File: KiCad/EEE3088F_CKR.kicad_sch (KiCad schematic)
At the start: 0 parts

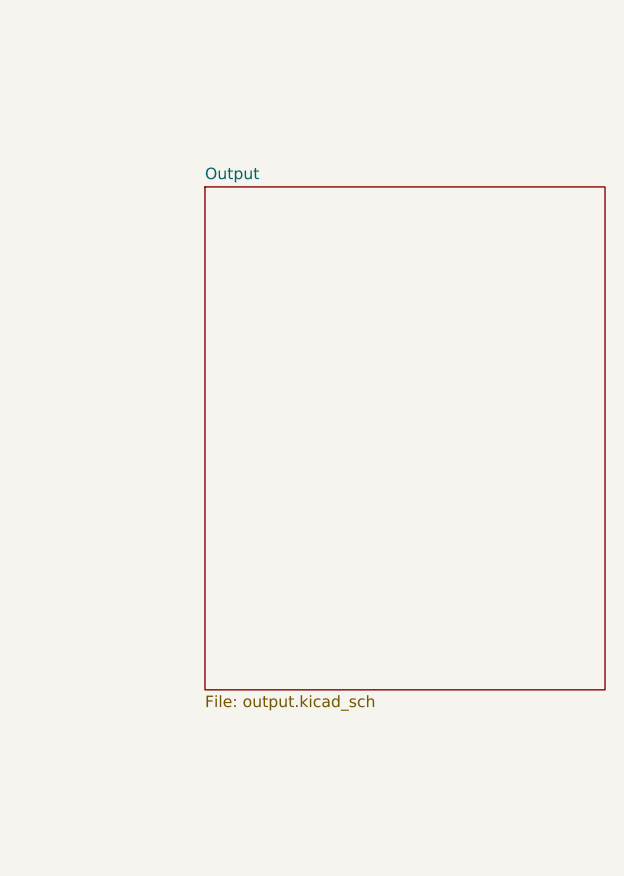
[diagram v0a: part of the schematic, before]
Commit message: added EEPROM
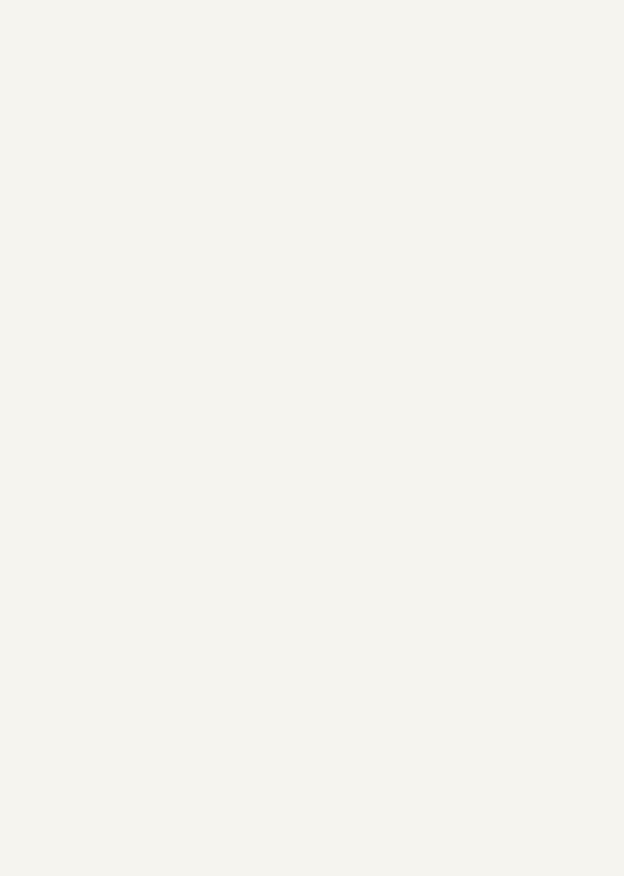
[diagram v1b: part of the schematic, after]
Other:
- removed sheet Output
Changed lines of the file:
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@@
 (kicad_sch (version 20230121) (generator eeschema)
   (paper "A4")
-  (sheet (at 210.82 77.47) (size 44.45 55.88) (fields_autoplaced)
-    (stroke (width 0.1524) (type solid))
-    (fill (color 0 0 0 0.0000))
-    (property "Sheetname" "Output" (at 210.82 76.7584 0)
-      (effects (font (size 1.27 1.27)) (justify left bottom))
-    )
-    (property "Sheetfile" "output.kicad_sch" (at 210.82 133.9346 0)
-      (effects (font (size 1.27 1.27)) (justify left top))
-    )
-    (instances
-      (project "EEE3088F_CKR"
-        (path "/31e5d740-f3fb-4029-be8d-dfdc4f653d72" (page "5"))
-      )
-    )
-  )
   (sheet (at 135.89 53.34) (size 33.02 95.25) (fields_autoplaced)
     (stroke (width 0.1524) (type solid))

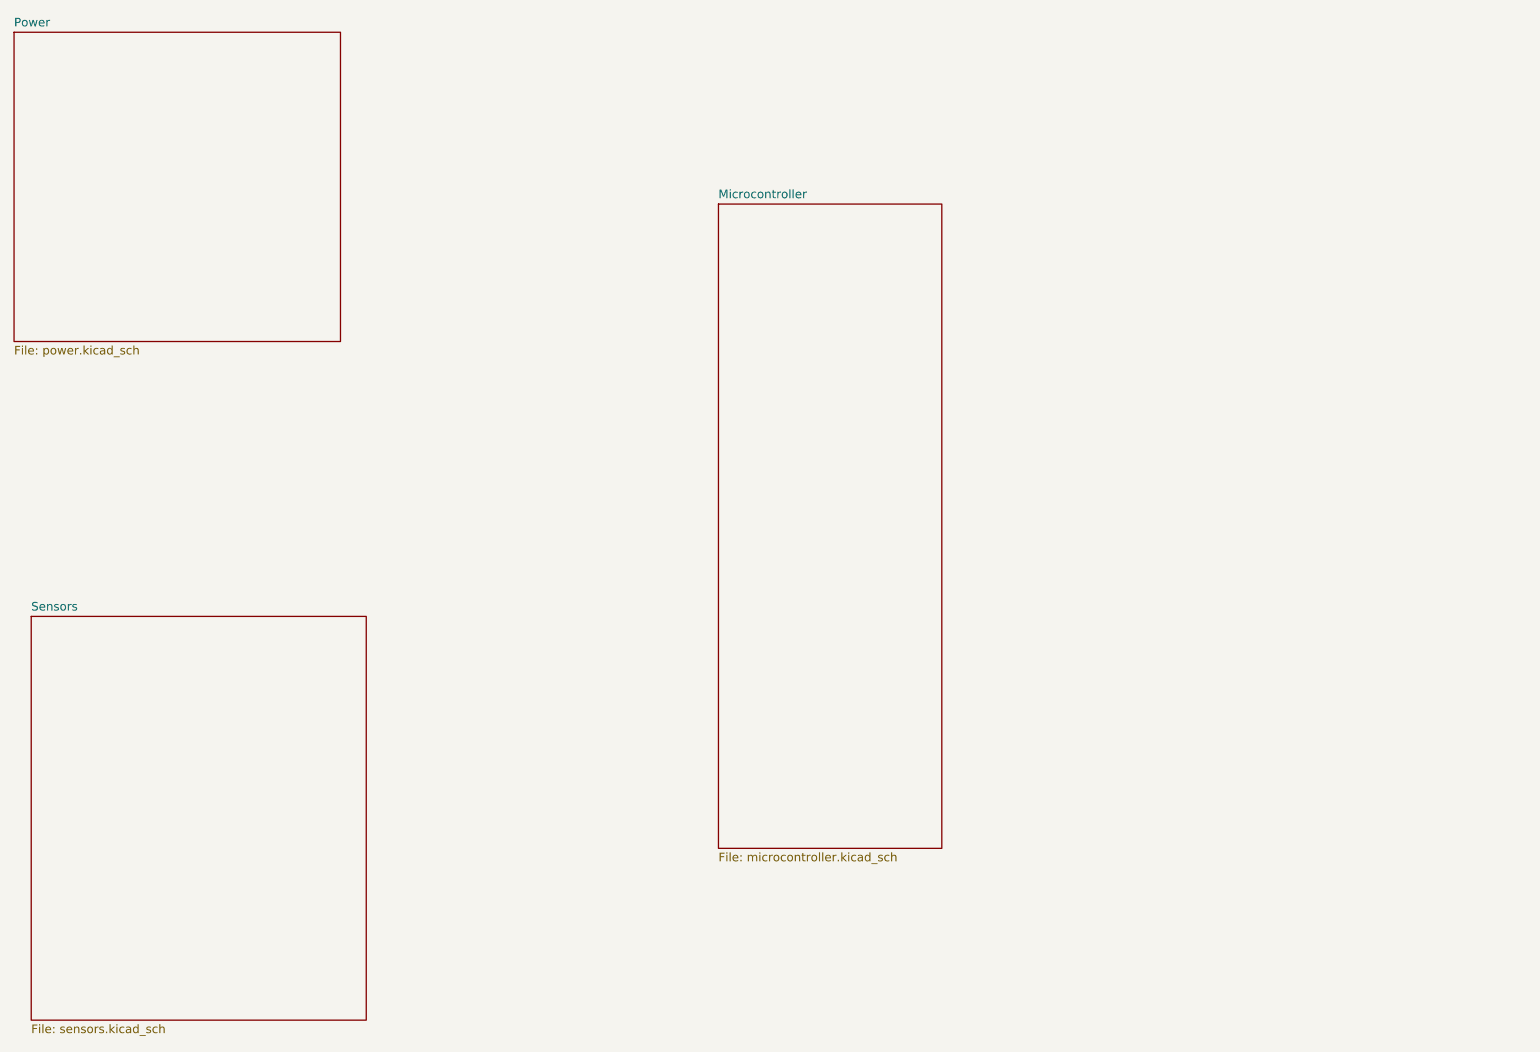
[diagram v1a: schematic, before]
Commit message: added heirachals and connected subsheets
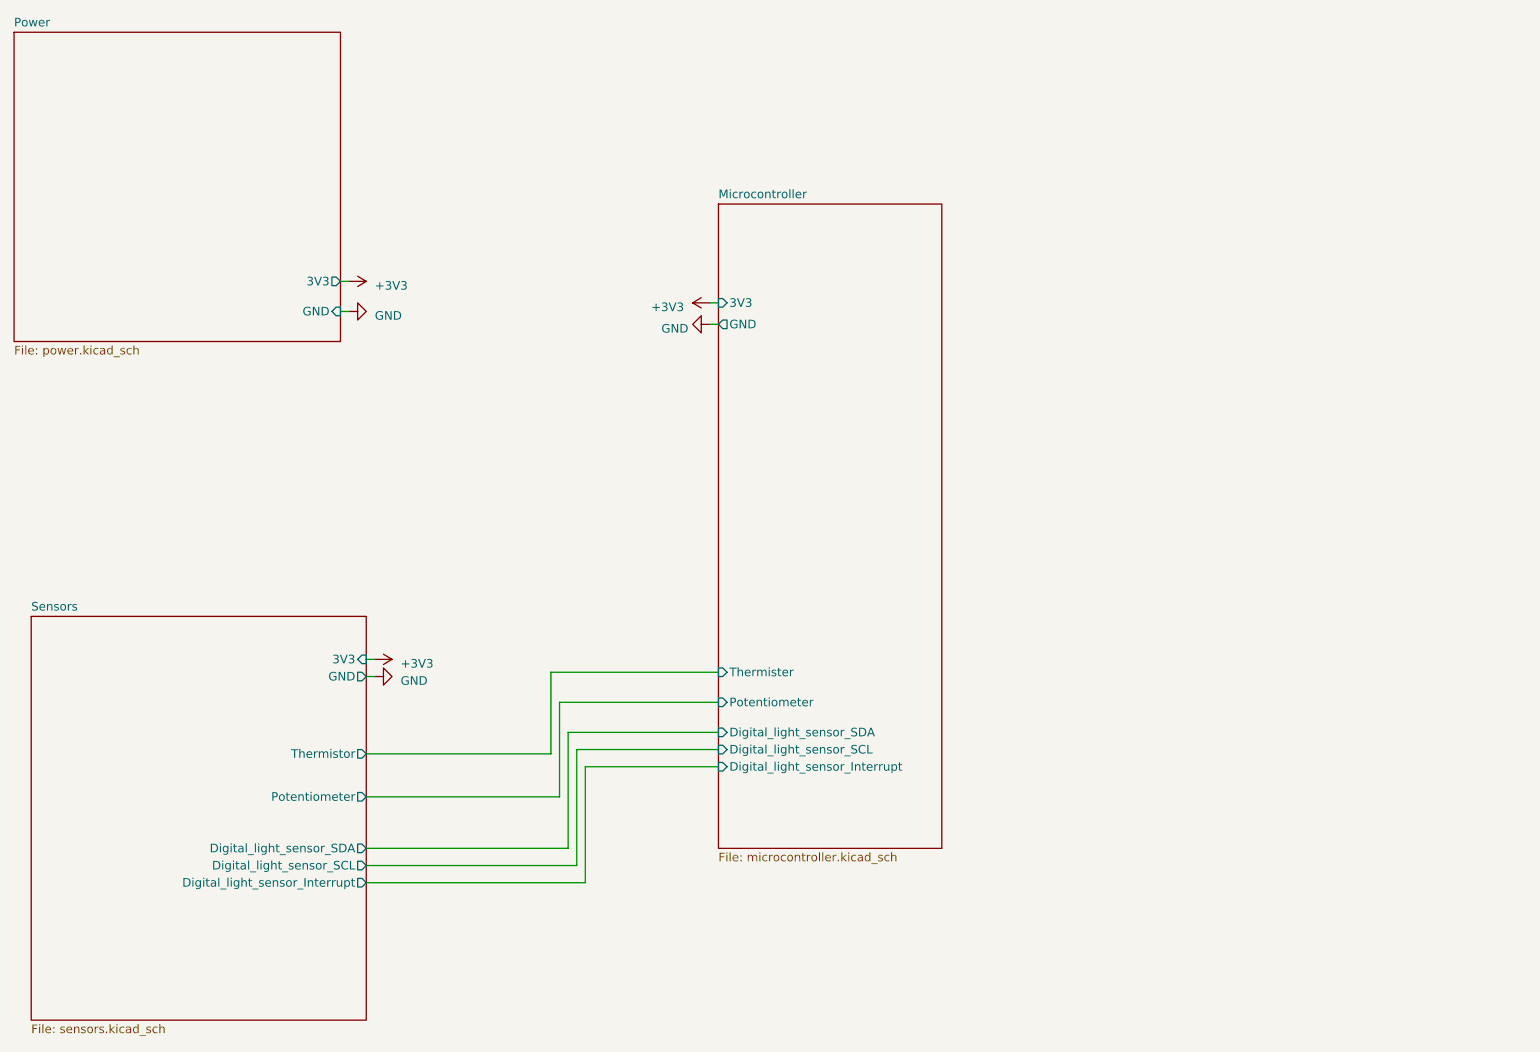
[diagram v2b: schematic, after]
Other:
- sheet Microcontroller ports: added 3V3, Digital_light_sensor_Interrupt, Digital_light_sensor_SCL, Digital_light_sensor_SDA, GND, Potentiometer, Thermister; removed none
- sheet Power ports: added 3V3, GND; removed none
- sheet Sensors ports: added 3V3, Digital_light_sensor_Interrupt, Digital_light_sensor_SCL, Digital_light_sensor_SDA, GND, Potentiometer, Thermistor; removed none
